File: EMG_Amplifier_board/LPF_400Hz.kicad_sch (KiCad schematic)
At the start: 5 parts, among them U1 LPV821DBVR

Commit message: add footprints
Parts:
- C10: renamed from C2; footprint Capacitor_SMD:C_0201_0603Metric -> Capacitor_SMD:C_1210_3225Metric
- R22: renamed from R1; value 27kOhm -> 27kR
- renumbered C1 to C9, R2 to R23
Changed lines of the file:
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@@
+		)
+	)
+	(hierarchical_label "GND"
+		(shape input)
+		(at 102.87 106.68 270)
+		(fields_autoplaced yes)
+		(effects
+			(font
+				(size 1.27 1.27)
+			)
+			(justify right)
 		)
 	)
@@
 	)
 	(symbol
-		(lib_id "power:GND")
-		(at 102.87 106.68 0)
-		(unit 1)
-		(exclude_from_sim no)
-		(in_bom yes)
-		(on_board yes)
-		(dnp no)
-		(fields_autoplaced yes)
-		(property "Reference" "#PWR02"
-			(at 102.87 113.03 0)
-			(effects
-				(font
-					(size 1.27 1.27)
-				)
-				(hide yes)
-			)
-		)
-		(property "Value" "GND"
-			(at 102.87 111.76 0)
-			(effects
-				(font
-					(size 1.27 1.27)
-				)
-			)
-		)
-		(property "Footprint" ""
-			(at 102.87 106.68 0)
-			(effects
-				(font
-					(size 1.27 1.27)
-				)
-				(hide yes)
-			)
-		)
-		(property "Datasheet" ""
-			(at 102.87 106.68 0)
-			(effects
-				(font
-					(size 1.27 1.27)
-				)
-				(hide yes)
-			)
-		)
-		(property "Description" "Power symbol creates a global label with name \"GND\" , ground"
-			(at 102.87 106.68 0)
-			(effects
-				(font
-					(size 1.27 1.27)
-				)
-				(hide yes)
-			)
-		)
-		(pin "1"
-		)
-		(instances
-			(project "EMG_amplifier"
-				(path "/26861adc-1ddf-4c37-9f8b-8db1c0839771/d4e218fa-378d-4687-9a1c-375f73f5fef2"
-					(reference "#PWR02")
-					(unit 1)
-				)
-			)
-		)
-	)
-	(symbol
 		(lib_id "Device:C")
 		(at 128.27 64.77 90)
@@
 		(dnp no)
 		(fields_autoplaced yes)
-		(property "Reference" "C2"
+		(property "Reference" "C10"
 			(at 128.27 57.15 90)
 			(effects
@@
 			)
 		)
-		(property "Footprint" "Capacitor_SMD:C_0201_0603Metric"
+		(property "Footprint" "Capacitor_SMD:C_1210_3225Metric"
 			(at 132.08 63.8048 0)
 			(effects
@@
 			(project "EMG_amplifier"
 				(path "/26861adc-1ddf-4c37-9f8b-8db1c0839771/d4e218fa-378d-4687-9a1c-375f73f5fef2"
-					(reference "C2")
+					(reference "C10")
 					(unit 1)
 				)
@@
 		(dnp no)
 		(fields_autoplaced yes)
-		(property "Reference" "R2"
+		(property "Reference" "R23"
 			(at 118.11 83.8199 0)
 			(effects
@@
 			(project "EMG_amplifier"
 				(path "/26861adc-1ddf-4c37-9f8b-8db1c0839771/d4e218fa-378d-4687-9a1c-375f73f5fef2"
-					(reference "R2")
+					(reference "R23")
 					(unit 1)
 				)
@@
 		(dnp no)
 		(fields_autoplaced yes)
-		(property "Reference" "C1"
+		(property "Reference" "C9"
 			(at 106.68 96.5199 0)
 			(effects
@@
 			(project "EMG_amplifier"
 				(path "/26861adc-1ddf-4c37-9f8b-8db1c0839771/d4e218fa-378d-4687-9a1c-375f73f5fef2"
-					(reference "C1")
+					(reference "C9")
 					(unit 1)
 				)
@@
 		(on_board yes)
 		(dnp no)
-		(property "Reference" "R1"
+		(property "Reference" "R22"
 			(at 104.14 59.69 90)
 			(effects
@@
 			)
 		)
-		(property "Value" "27kOhm"
+		(property "Value" "27kR"
 			(at 107.95 61.976 90)
 			(effects
@@
 			(project "EMG_amplifier"
 				(path "/26861adc-1ddf-4c37-9f8b-8db1c0839771/d4e218fa-378d-4687-9a1c-375f73f5fef2"
-					(reference "R1")
-					(unit 1)
-				)
+					(reference "R22")
+					(unit 1)
+				)

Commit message: acomponents choice
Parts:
- C10: footprint Capacitor_SMD:C_1210_3225Metric -> Capacitor_SMD:C_0805_2012Metric
- C9: footprint Capacitor_SMD:C_0201_0603Metric -> Capacitor_SMD:C_0402_1005Metric
- R23: value 27kOhm -> 27kR
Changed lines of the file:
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@@
 			)
 		)
-		(property "Footprint" "Capacitor_SMD:C_1210_3225Metric"
+		(property "Footprint" "Capacitor_SMD:C_0805_2012Metric"
 			(at 132.08 63.8048 0)
 			(effects
@@
 			)
 		)
-		(property "Value" "27kOhm"
+		(property "Value" "27kR"
 			(at 118.11 86.3599 0)
 			(effects
@@
 			)
 		)
-		(property "Footprint" "Capacitor_SMD:C_0201_0603Metric"
+		(property "Footprint" "Capacitor_SMD:C_0402_1005Metric"
 			(at 103.8352 101.6 0)
 			(effects
@@
 		(dnp no)
 		(property "Reference" "R22"
-			(at 104.14 59.69 90)
+			(at 106.172 59.944 90)
 			(effects
 				(font
@@
 		)
 		(property "Value" "27kR"
-			(at 107.95 61.976 90)
+			(at 106.934 61.976 90)
 			(effects
 				(font

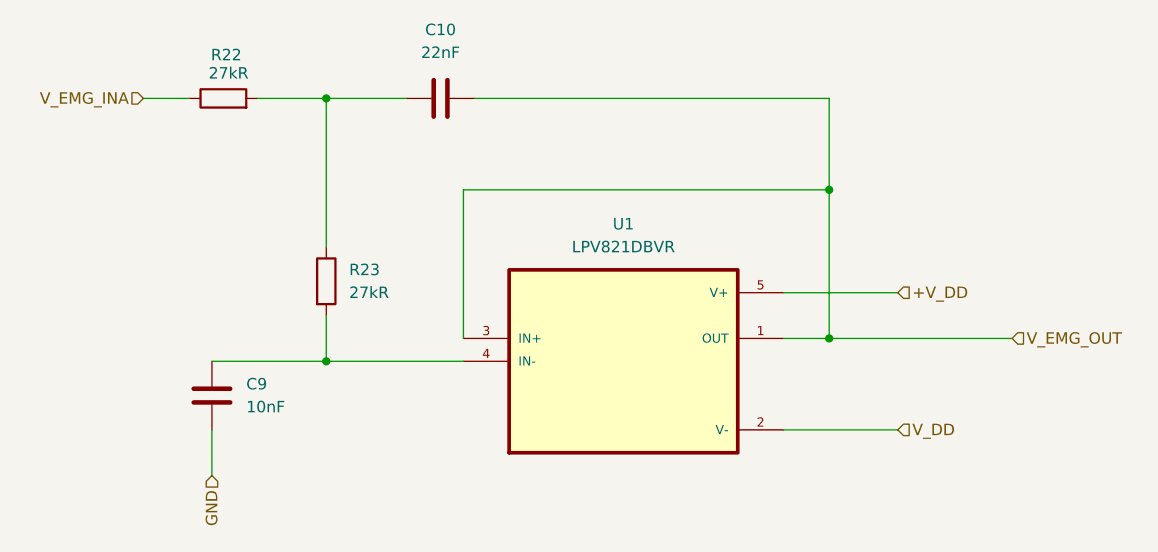
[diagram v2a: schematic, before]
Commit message: update the schematic with shared grounds and pin connectors
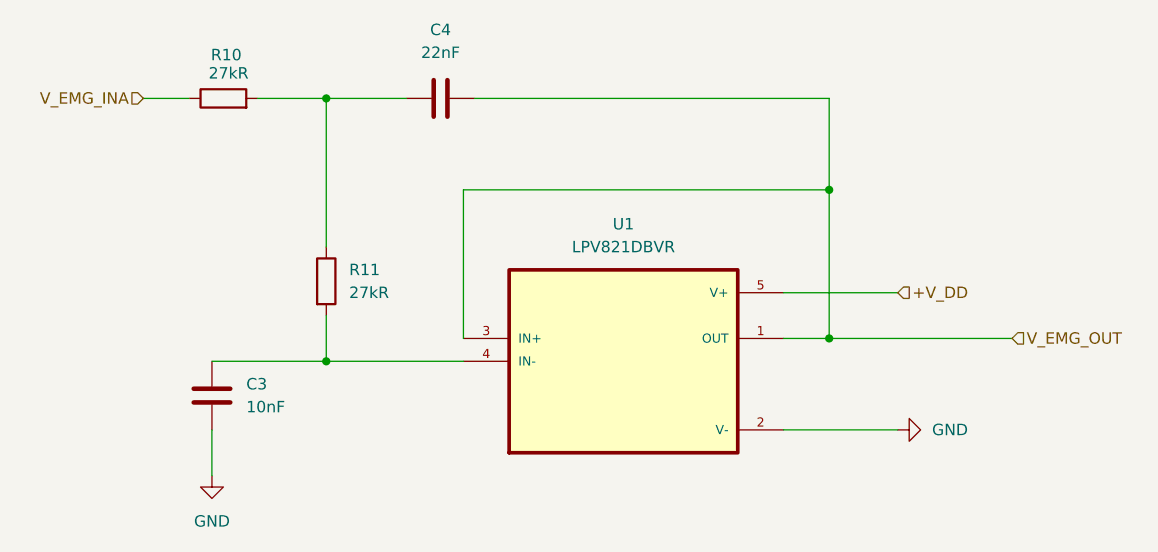
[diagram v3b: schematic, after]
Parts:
- renumbered C9 to C3, C10 to C4, R22 to R10, R23 to R11
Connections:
- net V_DD is gone; now on net GND: U1.2 (V-)
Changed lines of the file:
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@@
 		)
 	)
-	(hierarchical_label "V_DD"
+	(hierarchical_label "V_EMG_OUT"
 		(shape input)
-		(at 179.07 101.6 0)
+		(at 191.77 91.44 0)
 		(fields_autoplaced yes)
 		(effects
@@
 		)
 	)
-	(hierarchical_label "V_EMG_OUT"
+	(hierarchical_label "+V_DD"
 		(shape input)
-		(at 191.77 91.44 0)
+		(at 179.07 86.36 0)
 		(fields_autoplaced yes)
 		(effects
@@
 		)
 	)
-	(hierarchical_label "GND"
+	(hierarchical_label "V_EMG_INA"
 		(shape input)
-		(at 102.87 106.68 270)
+		(at 95.25 64.77 180)
 		(fields_autoplaced yes)
 		(effects
@@
 		)
 	)
-	(hierarchical_label "+V_DD"
-		(shape input)
-		(at 179.07 86.36 0)
-		(fields_autoplaced yes)
-		(effects
-			(font
-				(size 1.27 1.27)
-			)
-			(justify left)
-		)
-	)
-	(hierarchical_label "V_EMG_INA"
-		(shape input)
-		(at 95.25 64.77 180)
-		(fields_autoplaced yes)
-		(effects
-			(font
-				(size 1.27 1.27)
-			)
-			(justify right)
+	(symbol
+		(lib_id "power:GND")
+		(at 102.87 106.68 0)
+		(unit 1)
+		(exclude_from_sim no)
+		(in_bom yes)
+		(on_board yes)
+		(dnp no)
+		(fields_autoplaced yes)
+		(property "Reference" "#PWR02"
+			(at 102.87 113.03 0)
+			(effects
+				(font
+					(size 1.27 1.27)
+				)
+				(hide yes)
+			)
+		)
+		(property "Value" "GND"
+			(at 102.87 111.76 0)
+			(effects
+				(font
+					(size 1.27 1.27)
+				)
+			)
+		)
+		(property "Footprint" ""
+			(at 102.87 106.68 0)
+			(effects
+				(font
+					(size 1.27 1.27)
+				)
+				(hide yes)
+			)
+		)
+		(property "Datasheet" ""
+			(at 102.87 106.68 0)
+			(effects
+				(font
+					(size 1.27 1.27)
+				)
+				(hide yes)
+			)
+		)
+		(property "Description" "Power symbol creates a global label with name \"GND\" , ground"
+			(at 102.87 106.68 0)
+			(effects
+				(font
+					(size 1.27 1.27)
+				)
+				(hide yes)
+			)
+		)
+		(pin "1"
+		)
+		(instances
+			(project "EMG_amplifier"
+				(path "/26861adc-1ddf-4c37-9f8b-8db1c0839771/190e8daf-ffdb-4cbc-86a8-05377b040767/ed3c4e47-5bb3-4707-b5f4-6896a3a88613"
+					(reference "#PWR02")
+					(unit 1)
+				)
+			)
 		)
 	)
@@
 		(dnp no)
 		(fields_autoplaced yes)
-		(property "Reference" "C10"
+		(property "Reference" "C4"
 			(at 128.27 57.15 90)
 			(effects
@@
 		(instances
 			(project "EMG_amplifier"
-				(path "/26861adc-1ddf-4c37-9f8b-8db1c0839771/d4e218fa-378d-4687-9a1c-375f73f5fef2"
-					(reference "C10")
+				(path "/26861adc-1ddf-4c37-9f8b-8db1c0839771/190e8daf-ffdb-4cbc-86a8-05377b040767/ed3c4e47-5bb3-4707-b5f4-6896a3a88613"
+					(reference "C4")
 					(unit 1)
 				)
@@
 		(dnp no)
 		(fields_autoplaced yes)
-		(property "Reference" "R23"
+		(property "Reference" "R11"
 			(at 118.11 83.8199 0)
 			(effects
@@
 		(instances
 			(project "EMG_amplifier"
-				(path "/26861adc-1ddf-4c37-9f8b-8db1c0839771/d4e218fa-378d-4687-9a1c-375f73f5fef2"
-					(reference "R23")
+				(path "/26861adc-1ddf-4c37-9f8b-8db1c0839771/190e8daf-ffdb-4cbc-86a8-05377b040767/ed3c4e47-5bb3-4707-b5f4-6896a3a88613"
+					(reference "R11")
+					(unit 1)
+				)
+			)
+		)
+	)
+	(symbol
+		(lib_id "power:GND")
+		(at 179.07 101.6 90)
+		(unit 1)
+		(exclude_from_sim no)
+		(in_bom yes)
+		(on_board yes)
+		(dnp no)
+		(fields_autoplaced yes)
+		(property "Reference" "#PWR04"
+			(at 185.42 101.6 0)
+			(effects
+				(font
+					(size 1.27 1.27)
+				)
+				(hide yes)
+			)
+		)
+		(property "Value" "GND"
+			(at 182.88 101.5999 90)
+			(effects
+				(font
+					(size 1.27 1.27)
+				)
+				(justify right)
+			)
+		)
+		(property "Footprint" ""
+			(at 179.07 101.6 0)
+			(effects
+				(font
+					(size 1.27 1.27)
+				)
+				(hide yes)
+			)
+		)
+		(property "Datasheet" ""
+			(at 179.07 101.6 0)
+			(effects
+				(font
+					(size 1.27 1.27)
+				)
+				(hide yes)
+			)
+		)
+		(property "Description" "Power symbol creates a global label with name \"GND\" , ground"
+			(at 179.07 101.6 0)
+			(effects
+				(font
+					(size 1.27 1.27)
+				)
+				(hide yes)
+			)
+		)
+		(pin "1"
+		)
+		(instances
+			(project "EMG_amplifier"
+				(path "/26861adc-1ddf-4c37-9f8b-8db1c0839771/190e8daf-ffdb-4cbc-86a8-05377b040767/ed3c4e47-5bb3-4707-b5f4-6896a3a88613"
+					(reference "#PWR04")
 					(unit 1)
 				)
@@
 		(dnp no)
 		(fields_autoplaced yes)
-		(property "Reference" "C9"
+		(property "Reference" "C3"
 			(at 106.68 96.5199 0)
 			(effects
@@
 		(instances
 			(project "EMG_amplifier"
-				(path "/26861adc-1ddf-4c37-9f8b-8db1c0839771/d4e218fa-378d-4687-9a1c-375f73f5fef2"
-					(reference "C9")
+				(path "/26861adc-1ddf-4c37-9f8b-8db1c0839771/190e8daf-ffdb-4cbc-86a8-05377b040767/ed3c4e47-5bb3-4707-b5f4-6896a3a88613"
+					(reference "C3")
 					(unit 1)
 				)
@@
 		(on_board yes)
 		(dnp no)
-		(property "Reference" "R22"
+		(property "Reference" "R10"
 			(at 106.172 59.944 90)
 			(effects
@@
 		(instances
 			(project "EMG_amplifier"
-				(path "/26861adc-1ddf-4c37-9f8b-8db1c0839771/d4e218fa-378d-4687-9a1c-375f73f5fef2"
-					(reference "R22")
+				(path "/26861adc-1ddf-4c37-9f8b-8db1c0839771/190e8daf-ffdb-4cbc-86a8-05377b040767/ed3c4e47-5bb3-4707-b5f4-6896a3a88613"
+					(reference "R10")
 					(unit 1)
 				)
@@
 		(instances
 			(project "EMG_amplifier"
-				(path "/26861adc-1ddf-4c37-9f8b-8db1c0839771/d4e218fa-378d-4687-9a1c-375f73f5fef2"
+				(path "/26861adc-1ddf-4c37-9f8b-8db1c0839771/190e8daf-ffdb-4cbc-86a8-05377b040767/ed3c4e47-5bb3-4707-b5f4-6896a3a88613"
 					(reference "U1")
 					(unit 1)

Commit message: pcb design v1
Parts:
- added C11: 0.1uF, Capacitor_SMD:C_0805_2012Metric, symbol Device:C_Small
- R10, R11: footprint Resistor_SMD:R_0201_0603Metric -> Resistor_SMD:R_0402_1005Metric
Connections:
- net +V_DD: now also C11.1
- net GND: now also C11.2
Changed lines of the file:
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@@
+	)
+	(junction
+		(at 177.8 86.36)
+		(diameter 0)
+		(color 0 0 0 0)
 	)
 	(junction
@@
 	(wire
 		(pts
+			(xy 177.8 86.36) (xy 182.88 86.36)
+		)
+		(stroke
+			(width 0)
+			(type default)
+		)
+	)
+	(wire
+		(pts
 			(xy 171.45 91.44) (xy 191.77 91.44)
 		)
@@
 	(wire
 		(pts
-			(xy 166.37 86.36) (xy 179.07 86.36)
+			(xy 177.8 73.66) (xy 177.8 66.04)
+		)
+		(stroke
+			(width 0)
+			(type default)
+		)
+	)
+	(wire
+		(pts
+			(xy 166.37 86.36) (xy 177.8 86.36)
 		)
 		(stroke
@@
 		(pts
 			(xy 115.57 64.77) (xy 115.57 81.28)
+		)
+		(stroke
+			(width 0)
+			(type default)
+		)
+	)
+	(wire
+		(pts
+			(xy 177.8 78.74) (xy 177.8 86.36)
 		)
 		(stroke
@@
 	(hierarchical_label "+V_DD"
 		(shape input)
-		(at 179.07 86.36 0)
+		(at 182.88 86.36 0)
 		(fields_autoplaced yes)
 		(effects
@@
 			)
 		)
-		(property "Footprint" "Resistor_SMD:R_0201_0603Metric"
+		(property "Footprint" "Resistor_SMD:R_0402_1005Metric"
 			(at 113.792 85.09 90)
 			(effects
@@
 			)
 		)
-		(property "Footprint" "Resistor_SMD:R_0201_0603Metric"
+		(property "Footprint" "Resistor_SMD:R_0402_1005Metric"
 			(at 104.14 66.548 90)
 			(effects
@@
 					(unit 1)
 				)
+			)
+		)
+	)
+	(symbol
+		(lib_id "Device:C_Small")
+		(at 177.8 76.2 180)
+		(unit 1)
+		(exclude_from_sim no)
+		(in_bom yes)
+		(on_board yes)
+		(dnp no)
+		(property "Reference" "C11"
+			(at 183.134 74.93 0)
+			(effects
+				(font
+					(size 1.27 1.27)
+				)
+			)
+		)
+		(property "Value" "0.1uF"
+			(at 183.134 77.47 0)
+			(effects
+				(font
+					(size 1.27 1.27)
+				)
+			)
+		)
+		(property "Footprint" "Capacitor_SMD:C_0805_2012Metric"
+			(at 177.8 76.2 0)
+			(effects
+				(font
+					(size 1.27 1.27)
+				)
+				(hide yes)
+			)
+		)
+		(property "Datasheet" "~"
+			(at 177.8 76.2 0)
+			(effects
+				(font
+					(size 1.27 1.27)
+				)
+				(hide yes)
+			)
+		)
+		(property "Description" "Unpolarized capacitor, small symbol"
+			(at 177.8 76.2 0)
+			(effects
+				(font
+					(size 1.27 1.27)
+				)
+				(hide yes)
+			)
+		)
+		(pin "1"
+		)
+		(pin "2"
+		)
+		(instances
+			(project "EMG_amplifier"
+				(path "/26861adc-1ddf-4c37-9f8b-8db1c0839771/190e8daf-ffdb-4cbc-86a8-05377b040767/ed3c4e47-5bb3-4707-b5f4-6896a3a88613"
+					(reference "C11")
+					(unit 1)
+				)
+			)
+		)
+	)
+	(symbol
+		(lib_id "power:GND")
+		(at 177.8 66.04 180)
+		(unit 1)
+		(exclude_from_sim no)
+		(in_bom yes)
+		(on_board yes)
+		(dnp no)
+		(fields_autoplaced yes)
+		(property "Reference" "#PWR021"
+			(at 177.8 59.69 0)
+			(effects
+				(font
+					(size 1.27 1.27)
+				)
+				(hide yes)
+			)
+		)
+		(property "Value" "GND"
+			(at 177.7999 62.23 90)
+			(effects
+				(font
+					(size 1.27 1.27)
+				)
+				(justify right)
+			)
+		)
+		(property "Footprint" ""
+			(at 177.8 66.04 0)
+			(effects
+				(font
+					(size 1.27 1.27)
+				)
+				(hide yes)
+			)
+		)
+		(property "Datasheet" ""
+			(at 177.8 66.04 0)
+			(effects
+				(font
+					(size 1.27 1.27)
+				)
+				(hide yes)
+			)
+		)
+		(property "Description" "Power symbol creates a global label with name \"GND\" , ground"
+			(at 177.8 66.04 0)
+			(effects
+				(font
+					(size 1.27 1.27)
+				)
+				(hide yes)
+			)
+		)
+		(pin "1"
+		)
+		(instances
+			(project "EMG_amplifier"
+				(path "/26861adc-1ddf-4c37-9f8b-8db1c0839771/190e8daf-ffdb-4cbc-86a8-05377b040767/ed3c4e47-5bb3-4707-b5f4-6896a3a88613"
+					(reference "#PWR021")
+					(unit 1)
+				)

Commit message: first revision
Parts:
- R10, R11: value 27kR -> 27k
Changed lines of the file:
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@@
 			)
 		)
-		(property "Value" "27kR"
+		(property "Value" "27k"
 			(at 118.11 86.3599 0)
 			(effects
@@
 			)
 		)
-		(property "Value" "27kR"
+		(property "Value" "27k"
 			(at 106.934 61.976 90)
 			(effects

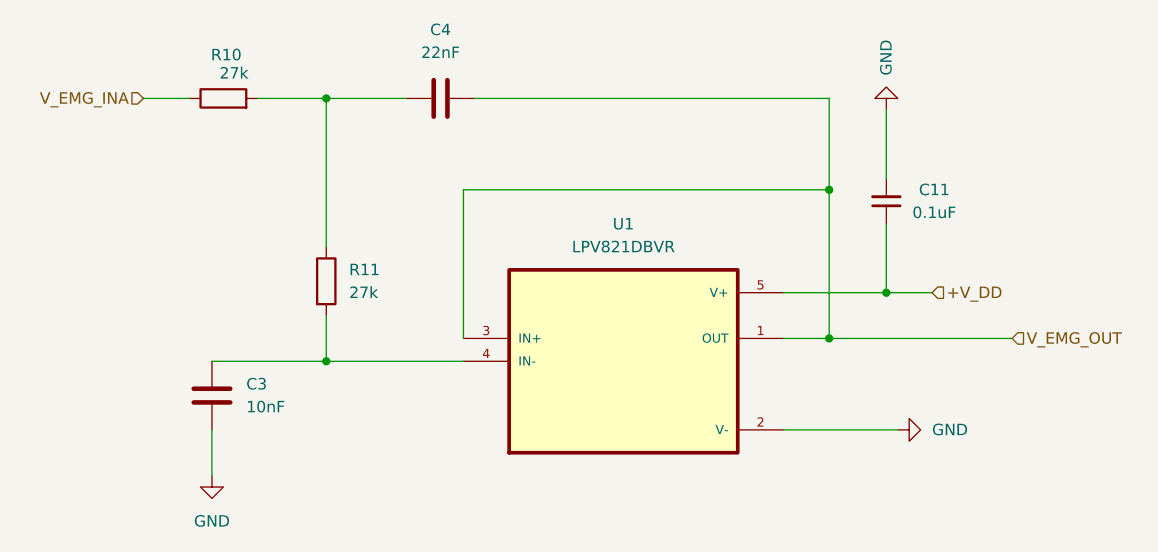
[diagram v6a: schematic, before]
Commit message: correct the 400Hz LPF schematic and InAmp trace routing
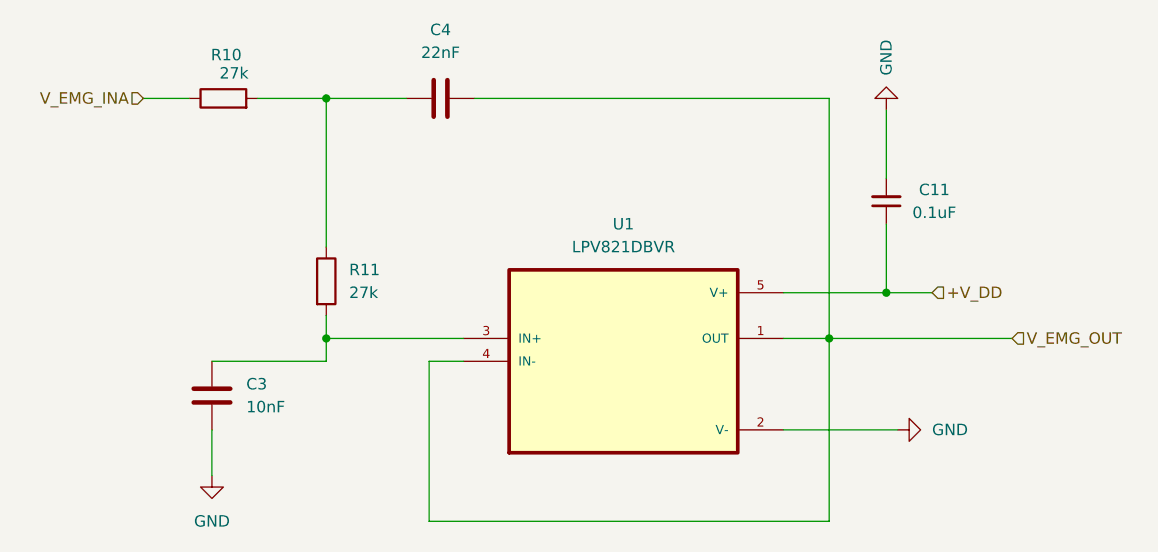
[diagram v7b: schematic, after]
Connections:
- net V_EMG_OUT: now also U1.4 (IN-); no longer U1.3 (IN+)
- net at C3.1, R11.2: now also U1.3 (IN+); no longer U1.4 (IN-)
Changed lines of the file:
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@@
 	(paper "A4")
 	(junction
-		(at 171.45 74.93)
+		(at 115.57 91.44)
 		(diameter 0)
 		(color 0 0 0 0)
@@
 		(color 0 0 0 0)
 	)
-	(junction
-		(at 115.57 93.98)
-		(diameter 0)
-		(color 0 0 0 0)
-	)
 	(wire
 		(pts
@@
 	(wire
 		(pts
+			(xy 127 111.76) (xy 127 93.98)
+		)
+		(stroke
+			(width 0)
+			(type default)
+		)
+	)
+	(wire
+		(pts
+			(xy 115.57 91.44) (xy 115.57 88.9)
+		)
+		(stroke
+			(width 0)
+			(type default)
+		)
+	)
+	(wire
+		(pts
 			(xy 177.8 86.36) (xy 182.88 86.36)
 		)
@@
 	(wire
 		(pts
-			(xy 115.57 93.98) (xy 130.81 93.98)
-		)
-		(stroke
-			(width 0)
-			(type default)
-		)
-	)
-	(wire
-		(pts
 			(xy 177.8 73.66) (xy 177.8 66.04)
 		)
@@
 	(wire
 		(pts
-			(xy 171.45 74.93) (xy 171.45 91.44)
+			(xy 171.45 64.77) (xy 171.45 91.44)
+		)
+		(stroke
+			(width 0)
+			(type default)
+		)
+	)
+	(wire
+		(pts
+			(xy 171.45 91.44) (xy 171.45 111.76)
 		)
 		(stroke
@@
 	(wire
 		(pts
-			(xy 171.45 64.77) (xy 171.45 74.93)
+			(xy 171.45 111.76) (xy 127 111.76)
 		)
 		(stroke
@@
 	(wire
 		(pts
-			(xy 115.57 93.98) (xy 115.57 88.9)
-		)
-		(stroke
-			(width 0)
-			(type default)
-		)
-	)
-	(wire
-		(pts
-			(xy 130.81 91.44) (xy 130.81 74.93)
+			(xy 115.57 93.98) (xy 115.57 91.44)
 		)
 		(stroke
@@
 	(wire
 		(pts
+			(xy 127 93.98) (xy 130.81 93.98)
+		)
+		(stroke
+			(width 0)
+			(type default)
+		)
+	)
+	(wire
+		(pts
 			(xy 177.8 78.74) (xy 177.8 86.36)
 		)
@@
 	(wire
 		(pts
-			(xy 130.81 74.93) (xy 171.45 74.93)
-		)
-		(stroke
+			(xy 115.57 91.44) (xy 130.81 91.44)
+		)
+		(stroke

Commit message: update R and C refs to correspond to paper
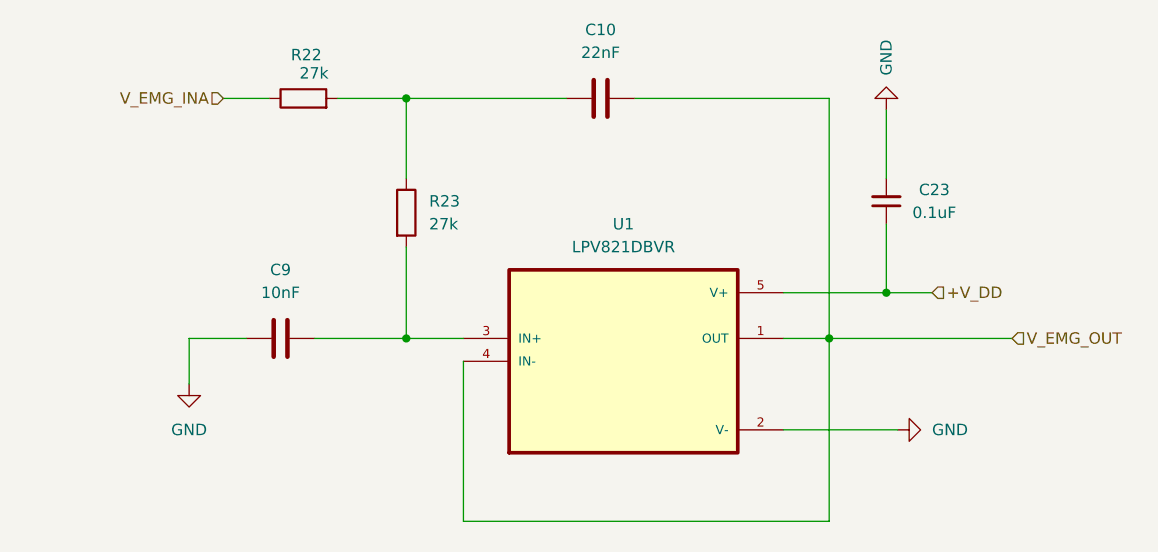
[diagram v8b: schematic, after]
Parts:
- renumbered C4 to C10, C11 to C23, C3 to C9, R10 to R22, R11 to R23
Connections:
- net GND: now also C9.1; no longer C9.2
- net at R23.2, U1.3 (IN+): now also C9.2; no longer C9.1
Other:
- moved on the sheet: C10, C9, R22, R23
